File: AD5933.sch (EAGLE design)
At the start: 76 parts, among them U1 ADG1604BRUZ, U10 ADP3303ARZ-3.3, U11 AD5242BRZ1M, U12 AD5245BRJZ100-R2, U2 AD5933YRSZ, U3 AD5242BRZ1M, U4 AD8606ARZ, U5 ADG1604BRUZ, U7 AD8606ARZ, U8 LTC6904MPMS8TRPBF, U9 ADP3303ARZ-3.3, X1 DC21MMX

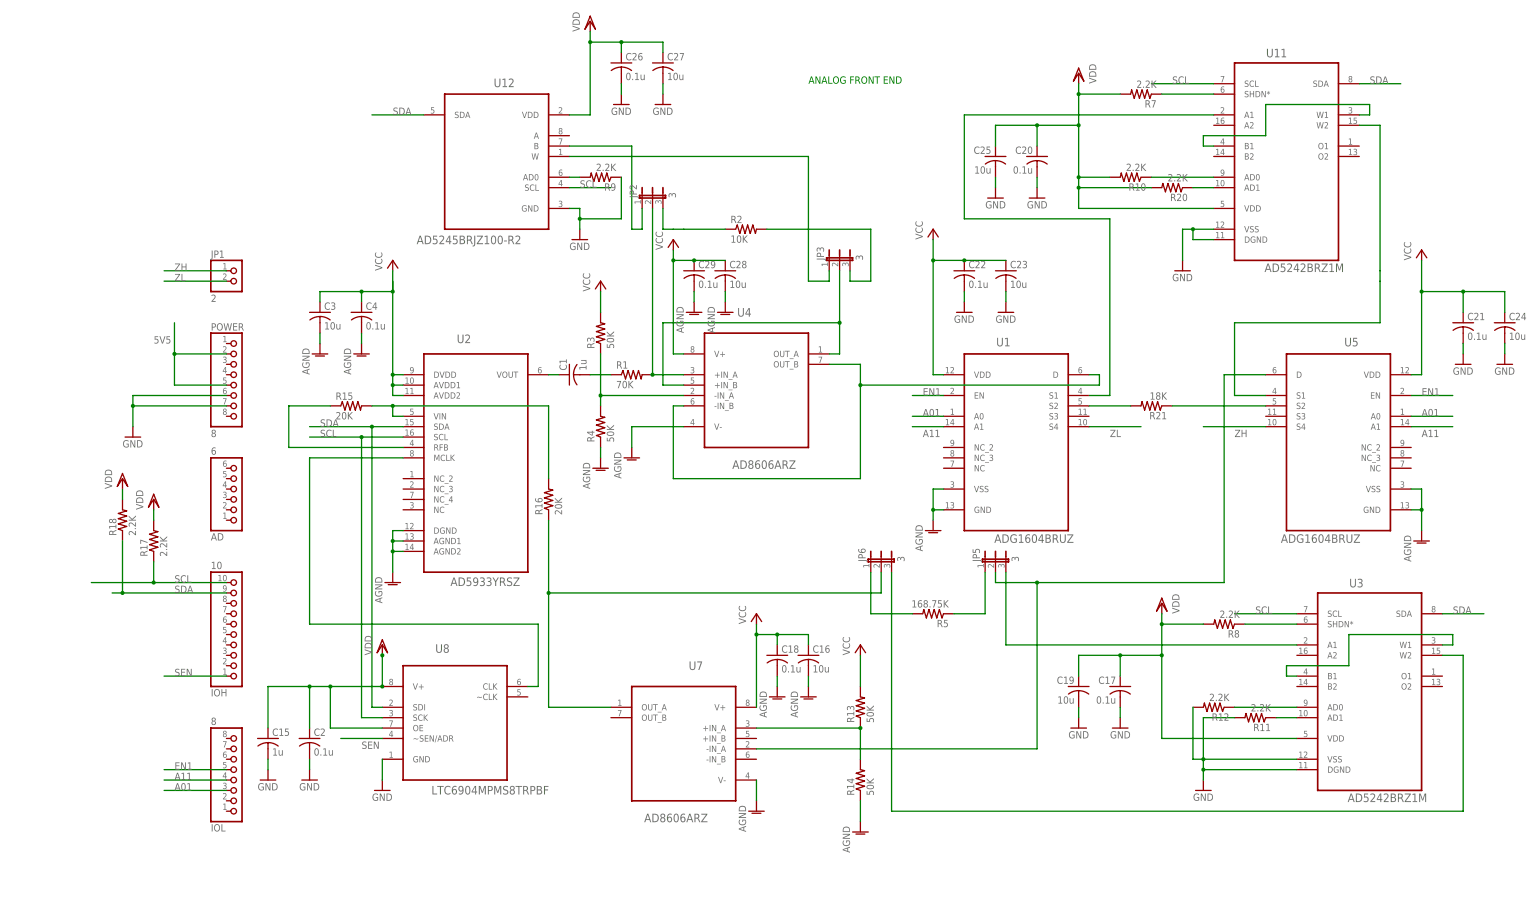
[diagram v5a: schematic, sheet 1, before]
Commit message: placed in shield area
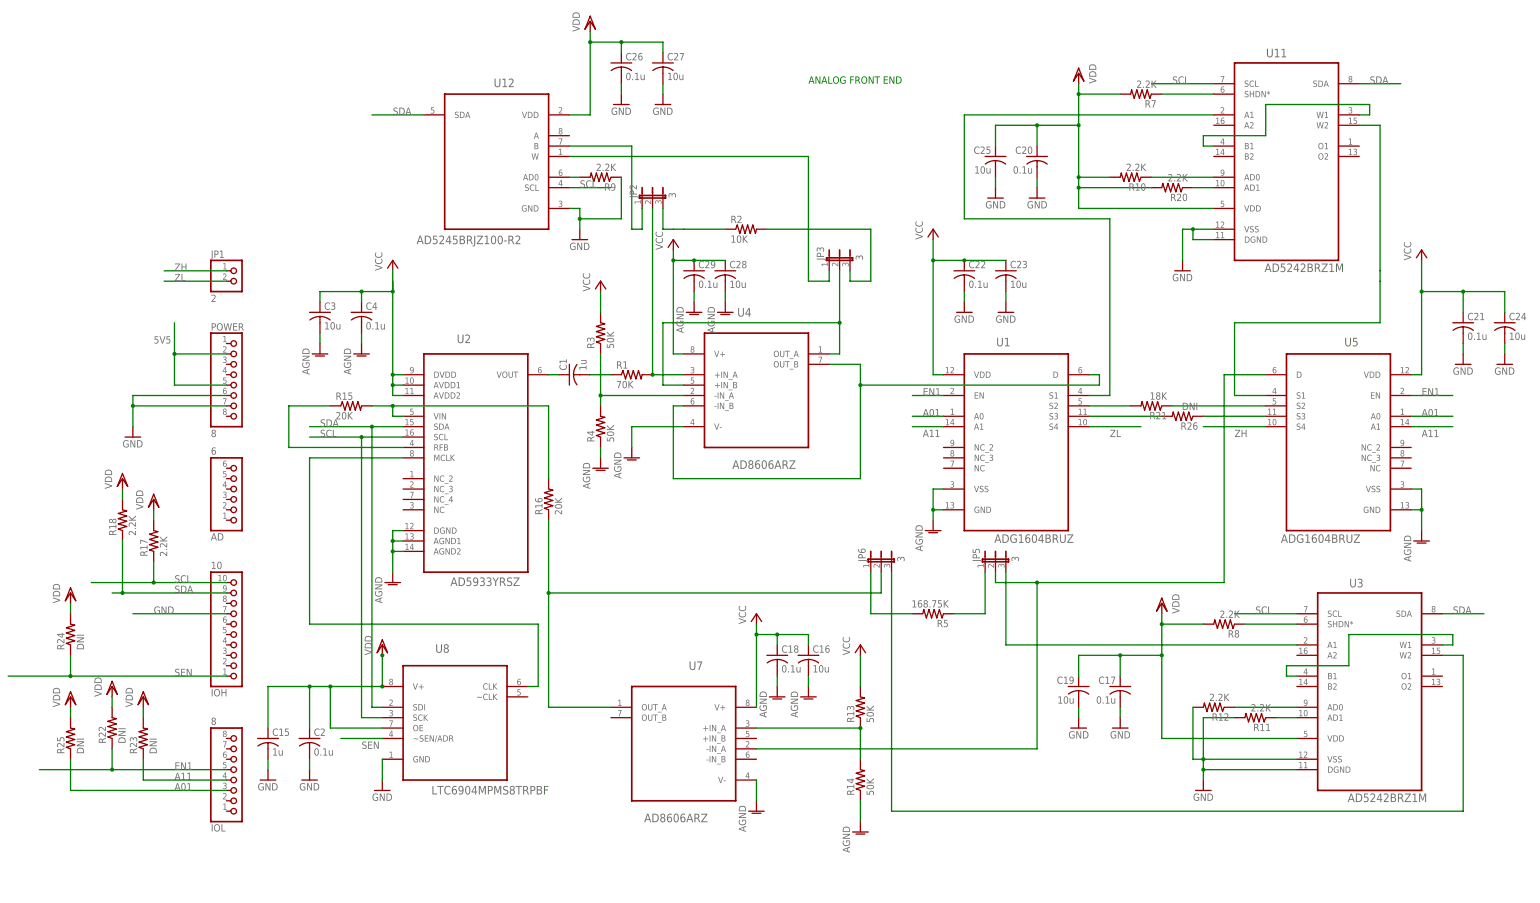
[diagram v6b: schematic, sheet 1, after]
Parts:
- removed PCB1: ARDUINO_MEGA2560, E14_Arduino_revC:ARDUINO_MEGA2560
- added R22, R23, R24, R25, R26: DNI, rcl:R-US_M0805
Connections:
- net N$12 renamed U7_INB-
- net N$13 renamed U5_S2
- net N$14 renamed U12_AD0
- net N$15 renamed U4_OUTB
- net N$16 renamed U7_INA+
- net N$17 renamed U2_RFB
- net N$18 renamed U2_MCLK
- net N$19 renamed U2_VIN
- net N$21 renamed U4_INA+
- net N$23 renamed U3_A1
- net N$24 renamed U11_W2
- net N$25 renamed U3_W1
- net N$26 renamed U3_AD0
- net N$27 renamed U3_W2
- net N$29 renamed U3_AD1
- net N$3 renamed U12_B
- net N$30 renamed U11_AD0
- net N$31 renamed U11_AD1
- net N$33 renamed U12_W
- net N$36 renamed PWR_INPUT
- net N$39 renamed U11_W1
- net N$4 renamed U4_OUTA
- net N$5 renamed U7_OUTA
- net N$6 renamed U4_INA-
- net N$8 renamed U1_S2
- net N$9 renamed U1_S1
- new net U1_S3: R26.2, U1.S3
- new net U5_S3: R26.1, U5.S3
- net A01: now also R25.1
- net A11: now also R23.1
- net EN1: now also R22.1
- net GND: now also IOH.7
- net SEN: now also R24.1
- net VDD: now also R22.2, R23.2, R24.2, R25.2
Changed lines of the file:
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@@
 <layer number="102" name="Vscore" color="7" fill="1" visible="no" active="yes"/>
 <layer number="103" name="tMap" color="7" fill="1" visible="yes" active="yes"/>
-<layer number="104" name="Name" color="7" fill="1" visible="no" active="yes"/>
+<layer number="104" name="Name" color="7" fill="1" visible="yes" active="yes"/>
 <layer number="105" name="tPlate" color="7" fill="1" visible="yes" active="yes"/>
 <layer number="106" name="bPlate" color="7" fill="1" visible="yes" active="yes"/>
@@
 <part name="P+7" library="supply1" deviceset="VCC" device=""/>
 <part name="P+8" library="supply1" deviceset="VCC" device=""/>
-<part name="PCB1" library="E14_Arduino_revC" deviceset="ARDUINO_MEGA2560" device=""/>
+<part name="R22" library="rcl" deviceset="R-US_" device="M0805" value="DNI"/>
+<part name="VDD3" library="supply1" deviceset="VDD" device=""/>
+<part name="R23" library="rcl" deviceset="R-US_" device="M0805" value="DNI"/>
+<part name="VDD4" library="supply1" deviceset="VDD" device=""/>
+<part name="R24" library="rcl" deviceset="R-US_" device="M0805" value="DNI"/>
+<part name="VDD5" library="supply1" deviceset="VDD" device=""/>
+<part name="R25" library="rcl" deviceset="R-US_" device="M0805" value="DNI"/>
+<part name="VDD6" library="supply1" deviceset="VDD" device=""/>
+<part name="R26" library="rcl" deviceset="R-US_" device="M0805" value="DNI"/>
 </parts>
 <sheets>
@@
 <instance part="P+7" gate="VCC" x="180.34" y="78.74"/>
 <instance part="P+8" gate="VCC" x="299.72" y="73.66"/>
+<instance part="R22" gate="G$1" x="-20.32" y="-43.18" rot="R90"/>
+<instance part="VDD3" gate="G$1" x="-20.32" y="-33.02"/>
+<instance part="R23" gate="G$1" x="-12.7" y="-45.72" rot="R90"/>
+<instance part="VDD4" gate="G$1" x="-12.7" y="-35.56"/>
+<instance part="R24" gate="G$1" x="-30.48" y="-20.32" rot="R90"/>
+<instance part="VDD5" gate="G$1" x="-30.48" y="-10.16"/>
+<instance part="R25" gate="G$1" x="-30.48" y="-45.72" rot="R90"/>
+<instance part="VDD6" gate="G$1" x="-30.48" y="-35.56"/>
+<instance part="R26" gate="G$1" x="241.3" y="33.02" rot="R180"/>
 </instances>
 <busses>
@@
 </segment>
 </net>
-<net name="N$4" class="0">
+<net name="U4_OUTA" class="0">
 <segment>
 <pinref part="U4" gate="A" pin="OUT_A"/>
@@
 </segment>
 </net>
-<net name="N$6" class="0">
+<net name="U4_INA-" class="0">
 <segment>
 <pinref part="R3" gate="G$1" pin="1"/>
@@
 <junction x="215.9" y="111.76"/>
 </segment>
-</net>
-<net name="N$8" class="0">
-<segment>
-<pinref part="U1" gate="A" pin="S2"/>
-<wire x1="218.44" y1="35.56" x2="228.6" y2="35.56" width="0.1524" layer="91"/>
-<pinref part="R21" gate="G$1" pin="2"/>
-</segment>
-</net>
-<net name="N$15" class="0">
+<segment>
+<pinref part="VDD3" gate="G$1" pin="VDD"/>
+<pinref part="R22" gate="G$1" pin="2"/>
+<wire x1="-20.32" y1="-35.56" x2="-20.32" y2="-38.1" width="0.1524" layer="91"/>
+</segment>
+<segment>
+<pinref part="VDD4" gate="G$1" pin="VDD"/>
+<pinref part="R23" gate="G$1" pin="2"/>
+<wire x1="-12.7" y1="-38.1" x2="-12.7" y2="-40.64" width="0.1524" layer="91"/>
+</segment>
+<segment>
+<pinref part="VDD5" gate="G$1" pin="VDD"/>
+<pinref part="R24" gate="G$1" pin="2"/>
+<wire x1="-30.48" y1="-12.7" x2="-30.48" y2="-15.24" width="0.1524" layer="91"/>
+</segment>
+<segment>
+<pinref part="VDD6" gate="G$1" pin="VDD"/>
+<pinref part="R25" gate="G$1" pin="2"/>
+<wire x1="-30.48" y1="-38.1" x2="-30.48" y2="-40.64" width="0.1524" layer="91"/>
+</segment>
+</net>
+<net name="U1_S3" class="0">
+<segment>
+<pinref part="R26" gate="G$1" pin="2"/>
+<pinref part="U1" gate="A" pin="S3"/>
+<wire x1="218.44" y1="33.02" x2="236.22" y2="33.02" width="0.1524" layer="91"/>
+</segment>
+</net>
+<net name="U4_OUTB" class="0">
 <segment>
 <pinref part="U1" gate="A" pin="D"/>
@@
 <segment>
 <pinref part="IOL" gate="A" pin="5"/>
-<wire x1="7.62" y1="-53.34" x2="-7.62" y2="-53.34" width="0.1524" layer="91"/>
 <label x="-5.08" y="-53.34" size="1.778" layer="95"/>
+<wire x1="7.62" y1="-53.34" x2="-20.32" y2="-53.34" width="0.1524" layer="91"/>
+<pinref part="R22" gate="G$1" pin="1"/>
+<wire x1="-20.32" y1="-53.34" x2="-38.1" y2="-53.34" width="0.1524" layer="91"/>
+<wire x1="-20.32" y1="-48.26" x2="-20.32" y2="-53.34" width="0.1524" layer="91"/>
+<junction x="-20.32" y="-53.34"/>
 </segment>
 </net>
@@
 <segment>
 <pinref part="IOL" gate="A" pin="3"/>
-<wire x1="7.62" y1="-58.42" x2="-7.62" y2="-58.42" width="0.1524" layer="91"/>
+<wire x1="7.62" y1="-58.42" x2="-27.94" y2="-58.42" width="0.1524" layer="91"/>
 <label x="-5.08" y="-58.42" size="1.778" layer="95"/>
+<wire x1="-27.94" y1="-58.42" x2="-30.48" y2="-58.42" width="0.1524" layer="91"/>
+<wire x1="-30.48" y1="-58.42" x2="-30.48" y2="-50.8" width="0.1524" layer="91"/>
+<pinref part="R25" gate="G$1" pin="1"/>
 </segment>
 </net>
@@
 <segment>
 <pinref part="IOL" gate="A" pin="4"/>
-<wire x1="7.62" y1="-55.88" x2="-7.62" y2="-55.88" width="0.1524" layer="91"/>
+<wire x1="7.62" y1="-55.88" x2="-12.7" y2="-55.88" width="0.1524" layer="91"/>
 <label x="-5.08" y="-55.88" size="1.778" layer="95"/>
-</segment>
-</net>
-<net name="N$16" class="0">
+<pinref part="R23" gate="G$1" pin="1"/>
+<wire x1="-12.7" y1="-55.88" x2="-12.7" y2="-50.8" width="0.1524" layer="91"/>
+</segment>
+</net>
+<net name="U7_INA+" class="0">
 <segment>
 <pinref part="R13" gate="G$1" pin="1"/>
@@
 </segment>
 </net>
-<net name="N$5" class="0">
+<net name="U7_OUTA" class="0">
 <segment>
 <wire x1="86.36" y1="-10.16" x2="167.64" y2="-10.16" width="0.1524" layer="91"/>
@@
 </segment>
 </net>
-<net name="N$19" class="0">
+<net name="U2_VIN" class="0">
 <segment>
 <pinref part="U2" gate="A" pin="VIN"/>
@@
 </segment>
 </net>
-<net name="N$17" class="0">
+<net name="U2_RFB" class="0">
 <segment>
 <pinref part="R15" gate="G$1" pin="1"/>
@@
 </segment>
 </net>
-<net name="N$18" class="0">
+<net name="U2_MCLK" class="0">
 <segment>
 <pinref part="U2" gate="A" pin="MCLK"/>
@@
 <segment>
 <pinref part="IOH" gate="A" pin="1"/>
-<wire x1="7.62" y1="-30.48" x2="-7.62" y2="-30.48" width="0.1524" layer="91"/>
+<wire x1="7.62" y1="-30.48" x2="-30.48" y2="-30.48" width="0.1524" layer="91"/>
 <label x="-5.08" y="-30.48" size="1.778" layer="95"/>
+<wire x1="-30.48" y1="-30.48" x2="-45.72" y2="-30.48" width="0.1524" layer="91"/>
+<pinref part="R24" gate="G$1" pin="1"/>
+<wire x1="-30.48" y1="-30.48" x2="-30.48" y2="-25.4" width="0.1524" layer="91"/>
+<junction x="-30.48" y="-30.48"/>
 </segment>
 </net>
@@
 </segment>
 </net>
-<net name="N$21" class="0">
+<net name="U4_INA+" class="0">
 <segment>
 <pinref part="U4" gate="A" pin="+IN_A"/>
@@
 </segment>
 </net>
-<net name="N$3" class="0">
+<net name="U12_B" class="0">
 <segment>
 <pinref part="U12" gate="A" pin="B"/>
@@
 </segment>
 </net>
-<net name="N$33" class="0">
+<net name="U12_W" class="0">
 <segment>
 <pinref part="U12" gate="A" pin="W"/>
@@
 <wire x1="45.72" y1="-50.8" x2="45.72" y2="-55.88" width="0.1524" layer="91"/>
 </segment>
+<segment>
+<pinref part="IOH" gate="A" pin="7"/>
+<wire x1="7.62" y1="-15.24" x2="-15.24" y2="-15.24" width="0.1524" layer="91"/>
+<label x="-10.16" y="-15.24" size="1.778" layer="95"/>
+</segment>
 </net>
 <net name="N$7" class="0">
@@
 </segment>
 </net>
-<net name="N$27" class="0">
+<net name="U3_W2" class="0">
 <segment>
 <pinref part="JP6" gate="1" pin="3"/>
@@
 </segment>
 </net>
-<net name="N$26" class="0">
+<net name="U3_AD0" class="0">
 <segment>
 <pinref part="U3" gate="A" pin="AD0"/>
@@
 </segment>
 </net>
-<net name="N$29" class="0">
+<net name="U3_AD1" class="0">
 <segment>
 <pinref part="U3" gate="A" pin="AD1"/>
@@
 </segment>
 </net>
-<net name="N$23" class="0">
+<net name="U3_A1" class="0">
 <segment>
 <pinref part="U3" gate="A" pin="A1"/>
@@
 </segment>
 </net>
-<net name="N$25" class="0">
+<net name="U3_W1" class="0">
 <segment>
 <pinref part="U3" gate="A" pin="W1"/>
@@
 </segment>
 </net>
-<net name="N$24" class="0">
+<net name="U11_W2" class="0">
 <segment>
 <pinref part="U11" gate="A" pin="W2"/>
@@
 </segment>
 </net>
-<net name="N$30" class="0">
+<net name="U11_AD0" class="0">
 <segment>
 <pinref part="U11" gate="A" pin="AD0"/>
@@
 </segment>
 </net>
-<net name="N$31" class="0">
+<net name="U11_AD1" class="0">
 <segment>
 <pinref part="U11" gate="A" pin="AD1"/>
@@
 </segment>
 </net>
-<net name="N$39" class="0">
+<net name="U11_W1" class="0">
 <segment>
 <pinref part="U11" gate="A" pin="W1"/>
@@
 </segment>
 </net>
-<net name="N$13" class="0">
+<net name="U5_S2" class="0">
 <segment>
 <pinref part="R21" gate="G$1" pin="1"/>
@@
 </segment>
 </net>
-<net name="N$9" class="0">
+<net name="U1_S1" class="0">
 <segment>
 <pinref part="U11" gate="A" pin="A1"/>
@@
 </segment>
 </net>
-<net name="N$12" class="0">
+<net name="U7_INB-" class="0">
 <segment>
 <pinref part="U5" gate="A" pin="D"/>
@@
 </segment>
 </net>
-<net name="N$14" class="0">
+<net name="U12_AD0" class="0">
 <segment>
 <pinref part="U12" gate="A" pin="AD0"/>
 <pinref part="R9" gate="G$1" pin="2"/>
 <wire x1="91.44" y1="91.44" x2="93.98" y2="91.44" width="0.1524" layer="91"/>
+</segment>
+</net>
+<net name="U1_S2" class="0">
+<segment>
+<pinref part="U1" gate="A" pin="S2"/>
+<wire x1="218.44" y1="35.56" x2="228.6" y2="35.56" width="0.1524" layer="91"/>
+<pinref part="R21" gate="G$1" pin="2"/>
+</segment>
+</net>
+<net name="U5_S3" class="0">
+<segment>
+<pinref part="U5" gate="A" pin="S3"/>
+<pinref part="R26" gate="G$1" pin="1"/>
+<wire x1="261.62" y1="33.02" x2="246.38" y2="33.02" width="0.1524" layer="91"/>
 </segment>
 </net>
@@
 </segment>
 </net>
-<net name="N$36" class="1">
+<net name="PWR_INPUT" class="1">
 <segment>
 <pinref part="U9" gate="A" pin="IN_2"/>
@@
 </plain>
 <instances>
-<instance part="PCB1" gate="G$1" x="68.58" y="50.8"/>
 </instances>
 <busses>

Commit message: Manual routing, add ground planes
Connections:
- net 5V5: no longer POWER.2
- net AGND: now also C21.2, C22.2, C23.2, C24.2
- net GND: no longer C21.2, C22.2, C23.2, C24.2
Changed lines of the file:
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@@
 <class number="0" name="default" width="0" drill="0.3048">
 </class>
-<class number="1" name="power 5v" width="0.3556" drill="0.4064">
+<class number="1" name="power 5v" width="0.762" drill="0.6096">
 </class>
 </classes>
@@
 <part name="GND17" library="supply1" deviceset="AGND" device=""/>
 <part name="GND29" library="supply1" deviceset="GND" device=""/>
-<part name="GND30" library="supply1" deviceset="GND" device=""/>
-<part name="GND31" library="supply1" deviceset="GND" device=""/>
 <part name="GND32" library="supply1" deviceset="GND" device=""/>
 <part name="GND33" library="supply1" deviceset="GND" device=""/>
 <part name="GND34" library="supply1" deviceset="AGND" device=""/>
 <part name="GND35" library="supply1" deviceset="AGND" device=""/>
-<part name="GND36" library="supply1" deviceset="GND" device=""/>
-<part name="GND37" library="supply1" deviceset="GND" device=""/>
 <part name="JP5" library="jumper" deviceset="JP2E" device="" value="3"/>
 <part name="JP6" library="jumper" deviceset="JP2E" device="" value="3"/>
@@
 <part name="VDD6" library="supply1" deviceset="VDD" device=""/>
 <part name="R26" library="rcl" deviceset="R-US_" device="M0805" value="DNI"/>
+<part name="GND30" library="supply1" deviceset="AGND" device=""/>
+<part name="GND31" library="supply1" deviceset="AGND" device=""/>
+<part name="GND36" library="supply1" deviceset="AGND" device=""/>
+<part name="GND37" library="supply1" deviceset="AGND" device=""/>
 </parts>
 <sheets>
@@
 <instance part="GND17" gate="VR1" x="121.92" y="58.42"/>
 <instance part="GND29" gate="1" x="17.78" y="-55.88"/>
-<instance part="GND30" gate="1" x="187.96" y="58.42"/>
-<instance part="GND31" gate="1" x="198.12" y="58.42"/>
 <instance part="GND32" gate="1" x="104.14" y="109.22"/>
 <instance part="GND33" gate="1" x="114.3" y="109.22"/>
 <instance part="GND34" gate="VR1" x="142.24" y="-35.56"/>
 <instance part="GND35" gate="VR1" x="149.86" y="-35.56"/>
-<instance part="GND36" gate="1" x="309.88" y="45.72"/>
-<instance part="GND37" gate="1" x="320.04" y="45.72"/>
 <instance part="JP5" gate="1" x="195.58" y="-2.54"/>
 <instance part="JP6" gate="1" x="167.64" y="-2.54"/>
@@
 <instance part="VDD6" gate="G$1" x="-30.48" y="-35.56"/>
 <instance part="R26" gate="G$1" x="241.3" y="33.02" rot="R180"/>
+<instance part="GND30" gate="VR1" x="187.96" y="55.88"/>
+<instance part="GND31" gate="VR1" x="198.12" y="55.88"/>
+<instance part="GND36" gate="VR1" x="309.88" y="43.18"/>
+<instance part="GND37" gate="VR1" x="320.04" y="43.18"/>
 </instances>
 <busses>
@@
 <pinref part="GND4" gate="VR1" pin="AGND"/>
 <wire x1="299.72" y1="5.08" x2="299.72" y2="10.16" width="0.1524" layer="91"/>
+</segment>
+<segment>
+<pinref part="C21" gate="G$1" pin="2"/>
+<pinref part="GND36" gate="VR1" pin="AGND"/>
+<wire x1="309.88" y1="45.72" x2="309.88" y2="50.8" width="0.1524" layer="91"/>
+</segment>
+<segment>
+<pinref part="C24" gate="G$1" pin="2"/>
+<pinref part="GND37" gate="VR1" pin="AGND"/>
+<wire x1="320.04" y1="45.72" x2="320.04" y2="50.8" width="0.1524" layer="91"/>
+</segment>
+<segment>
+<pinref part="C23" gate="G$1" pin="2"/>
+<pinref part="GND31" gate="VR1" pin="AGND"/>
+<wire x1="198.12" y1="58.42" x2="198.12" y2="63.5" width="0.1524" layer="91"/>
+</segment>
+<segment>
+<pinref part="C22" gate="G$1" pin="2"/>
+<pinref part="GND30" gate="VR1" pin="AGND"/>
+<wire x1="187.96" y1="58.42" x2="187.96" y2="63.5" width="0.1524" layer="91"/>
 </segment>
 </net>
@@
 <net name="5V5" class="1">
 <segment>
-<pinref part="POWER" gate="A" pin="2"/>
-<wire x1="7.62" y1="48.26" x2="-5.08" y2="48.26" width="0.1524" layer="91"/>
-<wire x1="-5.08" y1="48.26" x2="-5.08" y2="40.64" width="0.1524" layer="91"/>
 <pinref part="POWER" gate="A" pin="5"/>
 <wire x1="-5.08" y1="40.64" x2="7.62" y2="40.64" width="0.1524" layer="91"/>
-<wire x1="-5.08" y1="48.26" x2="-5.08" y2="55.88" width="0.1524" layer="91"/>
-<junction x="-5.08" y="48.26"/>
+<wire x1="-5.08" y1="40.64" x2="-5.08" y2="55.88" width="0.1524" layer="91"/>
 <label x="-10.16" y="50.8" size="1.778" layer="95"/>
 </segment>
@@
 </segment>
 <segment>
-<pinref part="C22" gate="G$1" pin="2"/>
-<pinref part="GND30" gate="1" pin="GND"/>
-<wire x1="187.96" y1="63.5" x2="187.96" y2="60.96" width="0.1524" layer="91"/>
-</segment>
-<segment>
-<pinref part="C23" gate="G$1" pin="2"/>
-<pinref part="GND31" gate="1" pin="GND"/>
-<wire x1="198.12" y1="63.5" x2="198.12" y2="60.96" width="0.1524" layer="91"/>
-</segment>
-<segment>
 <pinref part="C26" gate="G$1" pin="2"/>
 <pinref part="GND32" gate="1" pin="GND"/>
@@
 </segment>
 <segment>
-<pinref part="C21" gate="G$1" pin="2"/>
-<pinref part="GND36" gate="1" pin="GND"/>
-<wire x1="309.88" y1="50.8" x2="309.88" y2="48.26" width="0.1524" layer="91"/>
-</segment>
-<segment>
-<pinref part="C24" gate="G$1" pin="2"/>
-<pinref part="GND37" gate="1" pin="GND"/>
-<wire x1="320.04" y1="50.8" x2="320.04" y2="48.26" width="0.1524" layer="91"/>
-</segment>
-<segment>
